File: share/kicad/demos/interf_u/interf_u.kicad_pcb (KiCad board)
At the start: 2 copper layers, 115.6 x 108 mm, 25 parts, among them P1 DB25FEMELLE, U1 74LS245, U2 74LS688, U3 74LS541, U5 628128, U8 EP600, U9 4003APG120, X1 8MHz

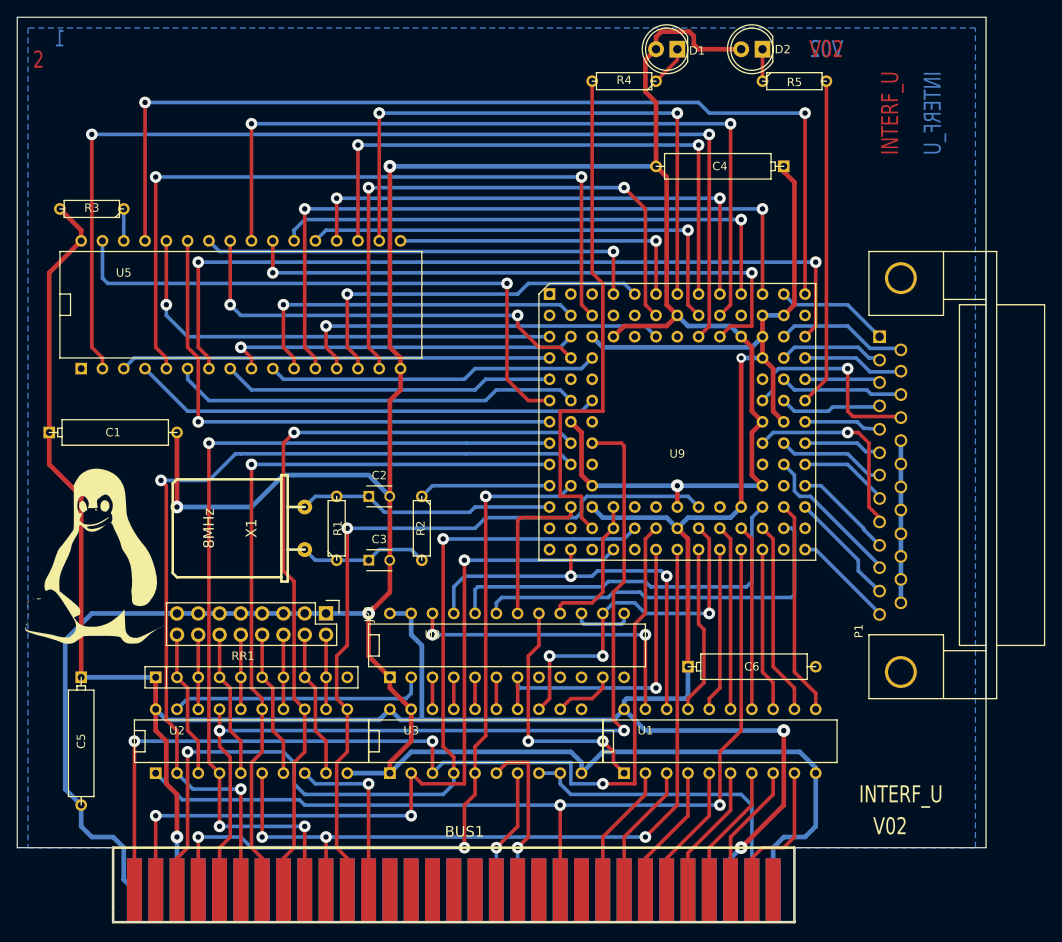
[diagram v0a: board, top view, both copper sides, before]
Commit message: Remove KiCad V4.0.7
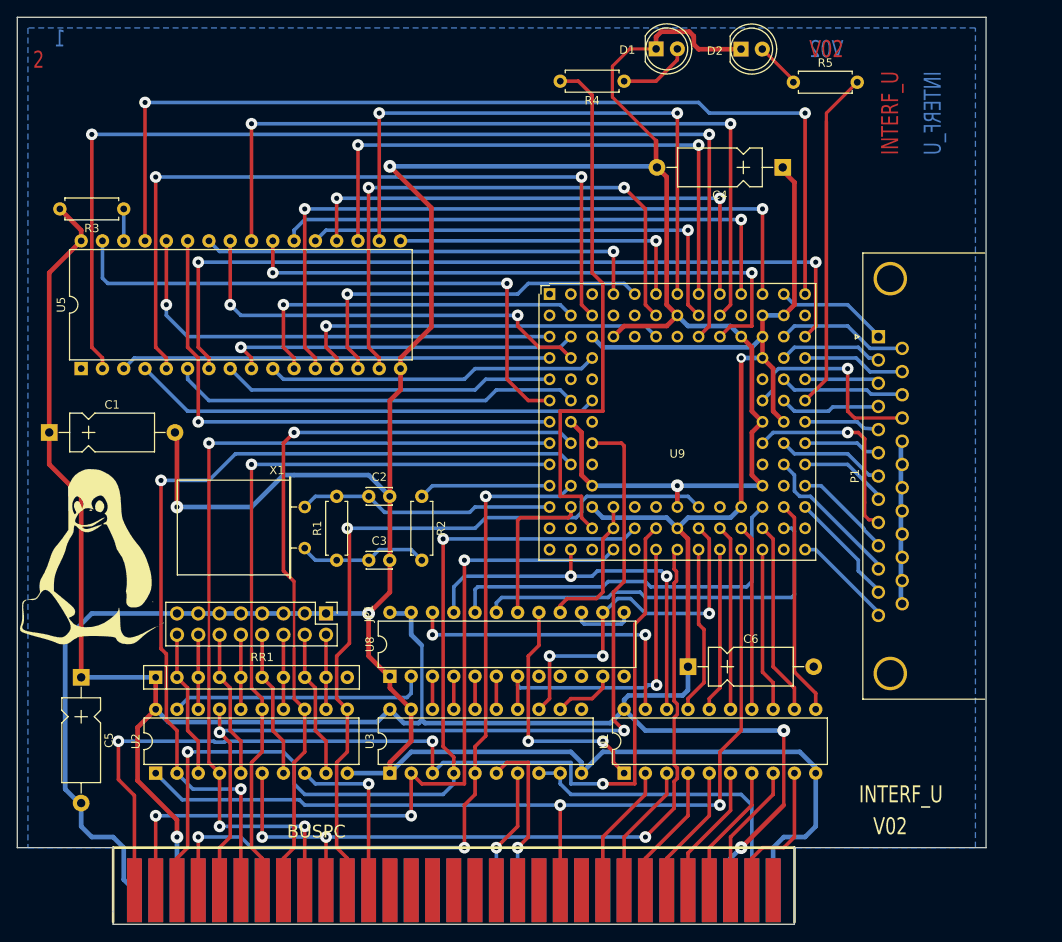
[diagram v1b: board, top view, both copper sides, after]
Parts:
- removed G***: LOGO, LOGO
- added G1: Tux, LOGO, F.Cu at (88.4, 98.6)
- BUS1: footprint BUS_PC -> interf_u:BUS_PC
- C1, C4, C5, C6: footprint Discret:CP6 -> Capacitor_THT:CP_Axial_L10.0mm_D4.5mm_P15.00mm_Horizontal
- C2, C3: footprint Capacitors_ThroughHole:C_Disc_D3_P2.5 -> Capacitor_THT:C_Disc_D3.0mm_W2.0mm_P2.50mm
- D1, D2: footprint LEDs:LED-5MM -> LED_THT:LED_D5.0mm
- JP1: footprint Pin_Headers:Pin_Header_Straight_2x08 -> Connector_PinHeader_2.54mm:PinHeader_2x08_P2.54mm_Vertical
- P1: footprint Connect:DB25FC -> Connector_Dsub:DSUB-25_Female_Horizontal_P2.77x2.84mm_EdgePinOffset9.90mm_Housed_MountingHolesOffset11.32mm
- R1, R2, R3, R4, R5: footprint Discret:R3 -> Resistor_THT:R_Axial_DIN0207_L6.3mm_D2.5mm_P7.62mm_Horizontal
- RR1: footprint Discret:r_pack9 -> Resistor_THT:R_Array_SIP10
- U1, U2, U3: footprint Sockets_DIP:DIP-20__300 -> Package_DIP:DIP-20_W7.62mm
- U5: footprint Sockets_DIP:DIP-32__600 -> Package_DIP:DIP-32_W15.24mm
- U8: footprint Sockets_DIP:DIP-24__300 -> Package_DIP:DIP-24_W7.62mm
- U9: footprint Sockets:PGA120 -> interf_u:PGA120
- X1: footprint HC-18UH -> Crystal:Crystal_HC18-U_Horizontal
- moved U5 20.5 mm to (87.0, 76.2), turned to 90 degrees
- moved P1 16.6 mm to (182.1, 72.4), turned to 90 degrees
- moved U8 14.4 mm to (123.8, 112.9), turned to 90 degrees
- moved U1 12.0 mm to (151.8, 124.5), turned to 90 degrees
- moved U2 12.0 mm to (95.9, 124.5), turned to 90 degrees
- moved U3 12.0 mm to (123.8, 124.5), turned to 90 degrees
- moved RR1 11.4 mm to (95.9, 113.0)
- moved C1 7.62 mm to (83.2, 83.8)
- moved C5 7.62 mm to (87.0, 113.0)
- moved C6 7.62 mm to (159.4, 111.8)
- moved C4 7.49 mm to (170.7, 52.2)
- moved R1 3.81 mm to (117.5, 99.1)
- moved R2 3.81 mm to (127.6, 91.4)
- moved R3 3.81 mm to (92.1, 57.1)
- moved D2 2.57 mm to (165.7, 38.1), turned to 0 degrees
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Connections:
- BUS1 pad 10: (no net) -> Net-(BUS1-Pad10)
- BUS1 pad 11: (no net) -> Net-(BUS1-Pad11)
- BUS1 pad 12: (no net) -> Net-(BUS1-Pad12)
- BUS1 pad 15: (no net) -> Net-(BUS1-Pad15)
- BUS1 pad 16: (no net) -> Net-(BUS1-Pad16)
- BUS1 pad 17: (no net) -> Net-(BUS1-Pad17)
- BUS1 pad 18: (no net) -> Net-(BUS1-Pad18)
- BUS1 pad 19: (no net) -> Net-(BUS1-Pad19)
- BUS1 pad 20: (no net) -> Net-(BUS1-Pad20)
- BUS1 pad 21: (no net) -> Net-(BUS1-Pad21)
- BUS1 pad 22: (no net) -> Net-(BUS1-Pad22)
- BUS1 pad 23: (no net) -> Net-(BUS1-Pad23)
- BUS1 pad 24: (no net) -> Net-(BUS1-Pad24)
- BUS1 pad 25: (no net) -> Net-(BUS1-Pad25)
- BUS1 pad 26: (no net) -> Net-(BUS1-Pad26)
- BUS1 pad 27: (no net) -> Net-(BUS1-Pad27)
- BUS1 pad 28: (no net) -> Net-(BUS1-Pad28)
- BUS1 pad 30: (no net) -> Net-(BUS1-Pad30)
- BUS1 pad 32: (no net) -> Net-(BUS1-Pad32)
- BUS1 pad 4: (no net) -> Net-(BUS1-Pad4)
- BUS1 pad 41: (no net) -> Net-(BUS1-Pad41)
- BUS1 pad 43: (no net) -> Net-(BUS1-Pad43)
- BUS1 pad 44: (no net) -> Net-(BUS1-Pad44)
- BUS1 pad 45: (no net) -> Net-(BUS1-Pad45)
- BUS1 pad 46: (no net) -> Net-(BUS1-Pad46)
- BUS1 pad 47: (no net) -> Net-(BUS1-Pad47)
- BUS1 pad 48: (no net) -> Net-(BUS1-Pad48)
- BUS1 pad 49: (no net) -> Net-(BUS1-Pad49)
- BUS1 pad 5: (no net) -> Net-(BUS1-Pad5)
- BUS1 pad 50: (no net) -> Net-(BUS1-Pad50)
- BUS1 pad 6: (no net) -> Net-(BUS1-Pad6)
- BUS1 pad 7: (no net) -> Net-(BUS1-Pad7)
- BUS1 pad 8: (no net) -> Net-(BUS1-Pad8)
- BUS1 pad 9: (no net) -> Net-(BUS1-Pad9)
- D1 pad 1: Net-(D1-Pad1) -> GND
- D1 pad 2: GND -> Net-(D1-Pad2)
- D2 pad 1: Net-(D2-Pad1) -> GND
- D2 pad 2: GND -> Net-(D2-Pad2)
- R4 pad 1: Net-(D1-Pad1) -> Net-(D1-Pad2)
- R5 pad 1: Net-(D2-Pad1) -> Net-(D2-Pad2)
- RR1 pad 10: (no net) -> Net-(RR1-Pad10)
- U3 pad 11: (no net) -> Net-(U3-Pad11)
- U8 pad 10: (no net) -> Net-(U8-Pad10)
- U8 pad 8: (no net) -> Net-(U8-Pad8)
- U8 pad 9: (no net) -> Net-(U8-Pad9)
- U9 pad A1: (no net) -> Net-(U9-PadA1)
- U9 pad A2: (no net) -> Net-(U9-PadA2)
- U9 pad A3: (no net) -> Net-(U9-PadA3)
- U9 pad B1: (no net) -> Net-(U9-PadB1)
- U9 pad B10: (no net) -> Net-(U9-PadB10)
- U9 pad B13: (no net) -> Net-(U9-PadB13)
- U9 pad B4: (no net) -> Net-(U9-PadB4)
- U9 pad B5: (no net) -> Net-(U9-PadB5)
- U9 pad C5: (no net) -> Net-(U9-PadC5)
- U9 pad E11: (no net) -> Net-(U9-PadE11)
- U9 pad E2: (no net) -> Net-(U9-PadE2)
- U9 pad E3: (no net) -> Net-(U9-PadE3)
- U9 pad J11: (no net) -> Net-(U9-PadJ11)
- U9 pad J3: (no net) -> Net-(U9-PadJ3)
- U9 pad K12: (no net) -> Net-(U9-PadK12)
- U9 pad L5: (no net) -> Net-(U9-PadL5)
- U9 pad L6: (no net) -> Net-(U9-PadL6)
- U9 pad L9: (no net) -> Net-(U9-PadL9)
- U9 pad M1: (no net) -> Net-(U9-PadM1)
- U9 pad M2: (no net) -> Net-(U9-PadM2)
- U9 pad N1: (no net) -> Net-(U9-PadN1)
- U9 pad N12: (no net) -> Net-(U9-PadN12)
- U9 pad N3: (no net) -> Net-(U9-PadN3)
- U9 pad N5: (no net) -> Net-(U9-PadN5)
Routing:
- net Net-(D1-Pad2): track 0.00 -> 8.67 mm
- net GND: track 432.6 -> 440.8 mm
- net Net-(D2-Pad2): track 0.00 -> 5.49 mm
- net Net-(D1-Pad1): track 4.86 -> 0.00 mm
- net Net-(D2-Pad1): track 3.81 -> 0.00 mm
- net /LED1: track 62.0 -> 64.9 mm
- net /PC-A0: track 115.9 -> 118.7 mm
- net VCC: track 337.0 -> 339.4 mm
- net /LED2: track 39.2 -> 40.6 mm
- net /PC-A9: track 95.6 -> 96.4 mm
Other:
- board size 115.6 x 108 mm -> 115.6 x 108.2 mm
- net class Default removed
- net class Power removed
- rule pad_to_mask_clearance: 0.254 -> 0
